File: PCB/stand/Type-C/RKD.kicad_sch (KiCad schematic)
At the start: 65 parts, among them J1 USB_C_Receptacle_USB2.0, J10 Conn_01x04_Male, J11 Conn_02x06_Odd_Even, J12 Conn_01x06, J13 Conn_01x03, J14 Conn_01x04, J15 Conn_01x04, J2 Conn_02x02_Odd_Even, J3 Conn_02x04_Odd_Even, J4 Conn_02x02_Odd_Even, J5 Conn_02x04_Odd_Even, K1 Key, K2 Key, K3 Key, K4 Key, SW2 SW_DIP_x04, SW3 SW_Push, SW5 SW_Push, U1 W25Q32JV, U2 RP2040, U3 CH9329, U4 AMS1117-33, Y1 Crystal 12MHZ HC49, Y2 Crystal_GND24 12MHZ 3225

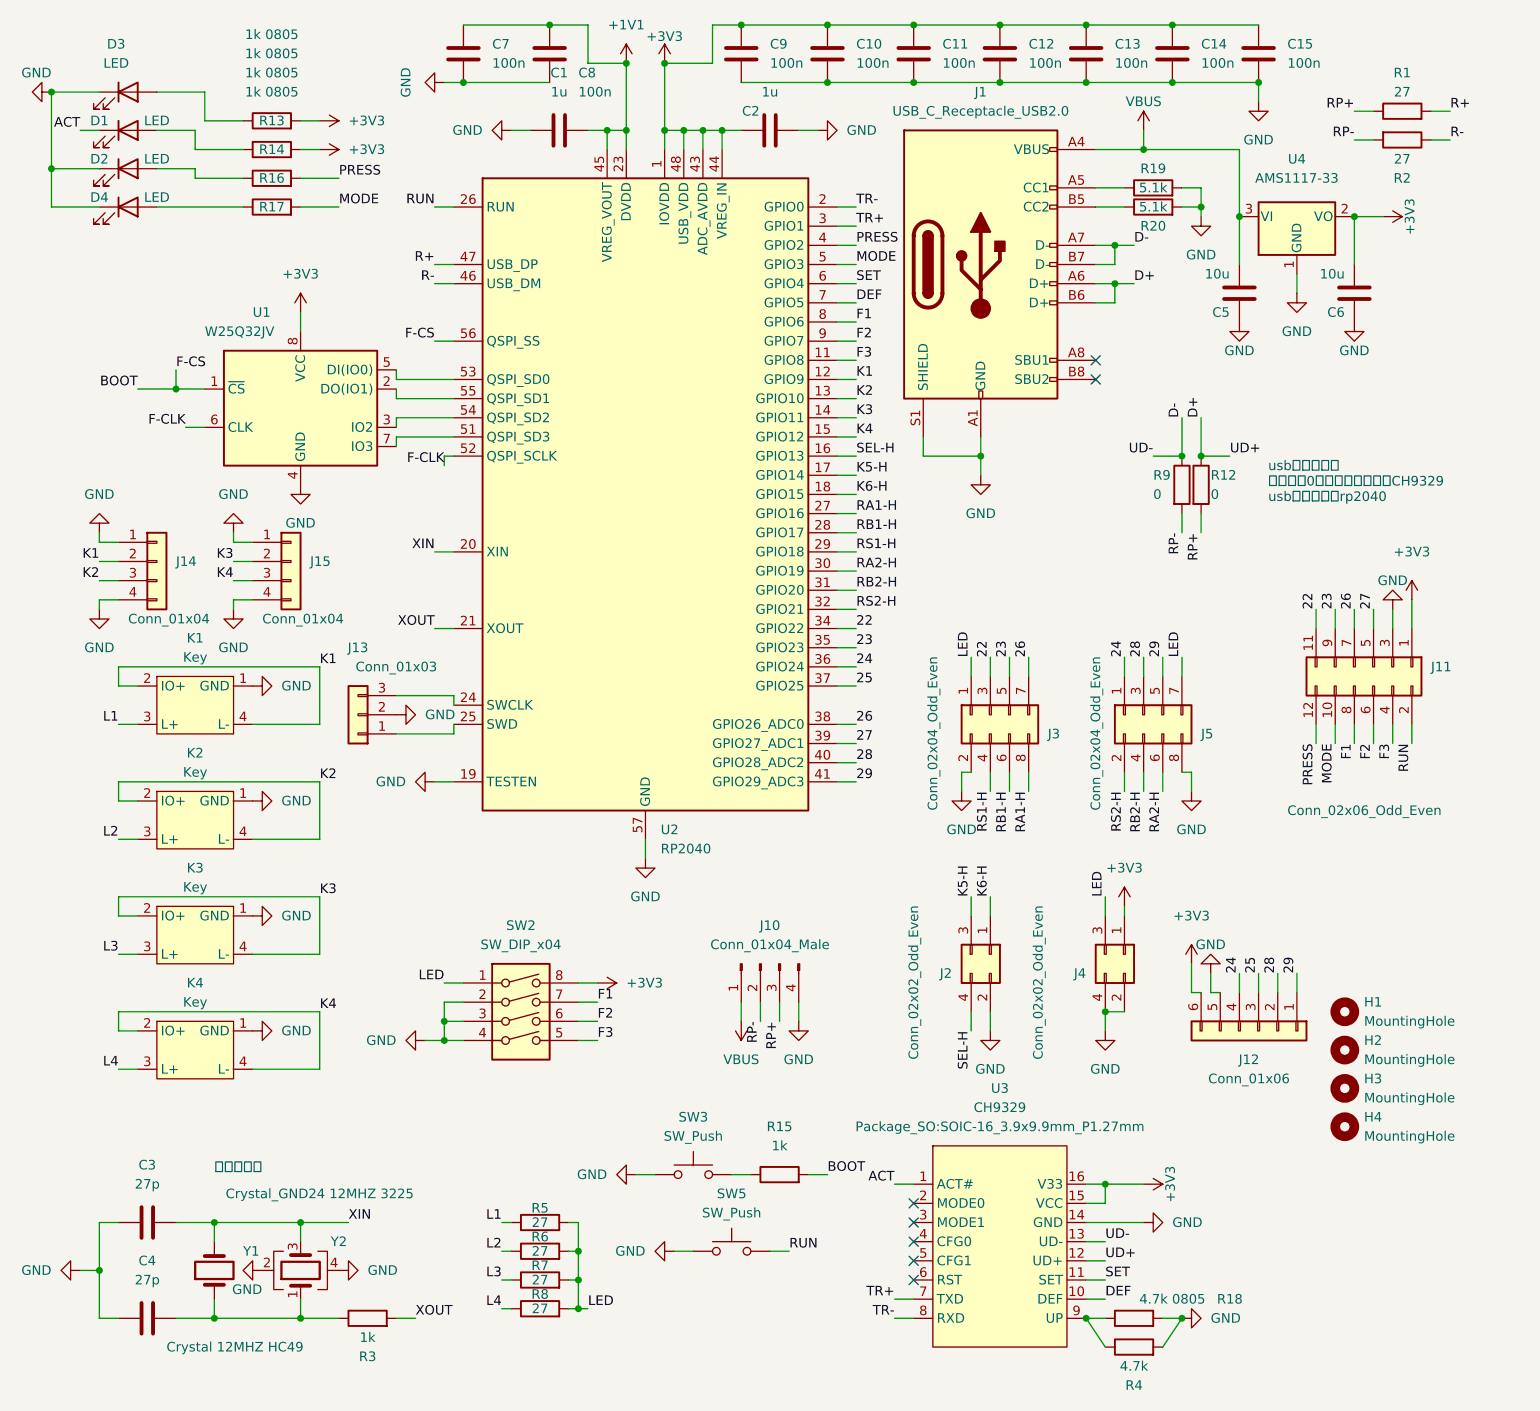
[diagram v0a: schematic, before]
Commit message: 紧急修复:经验证3225晶振无法稳定起振,故去除所以文件中的3225晶振
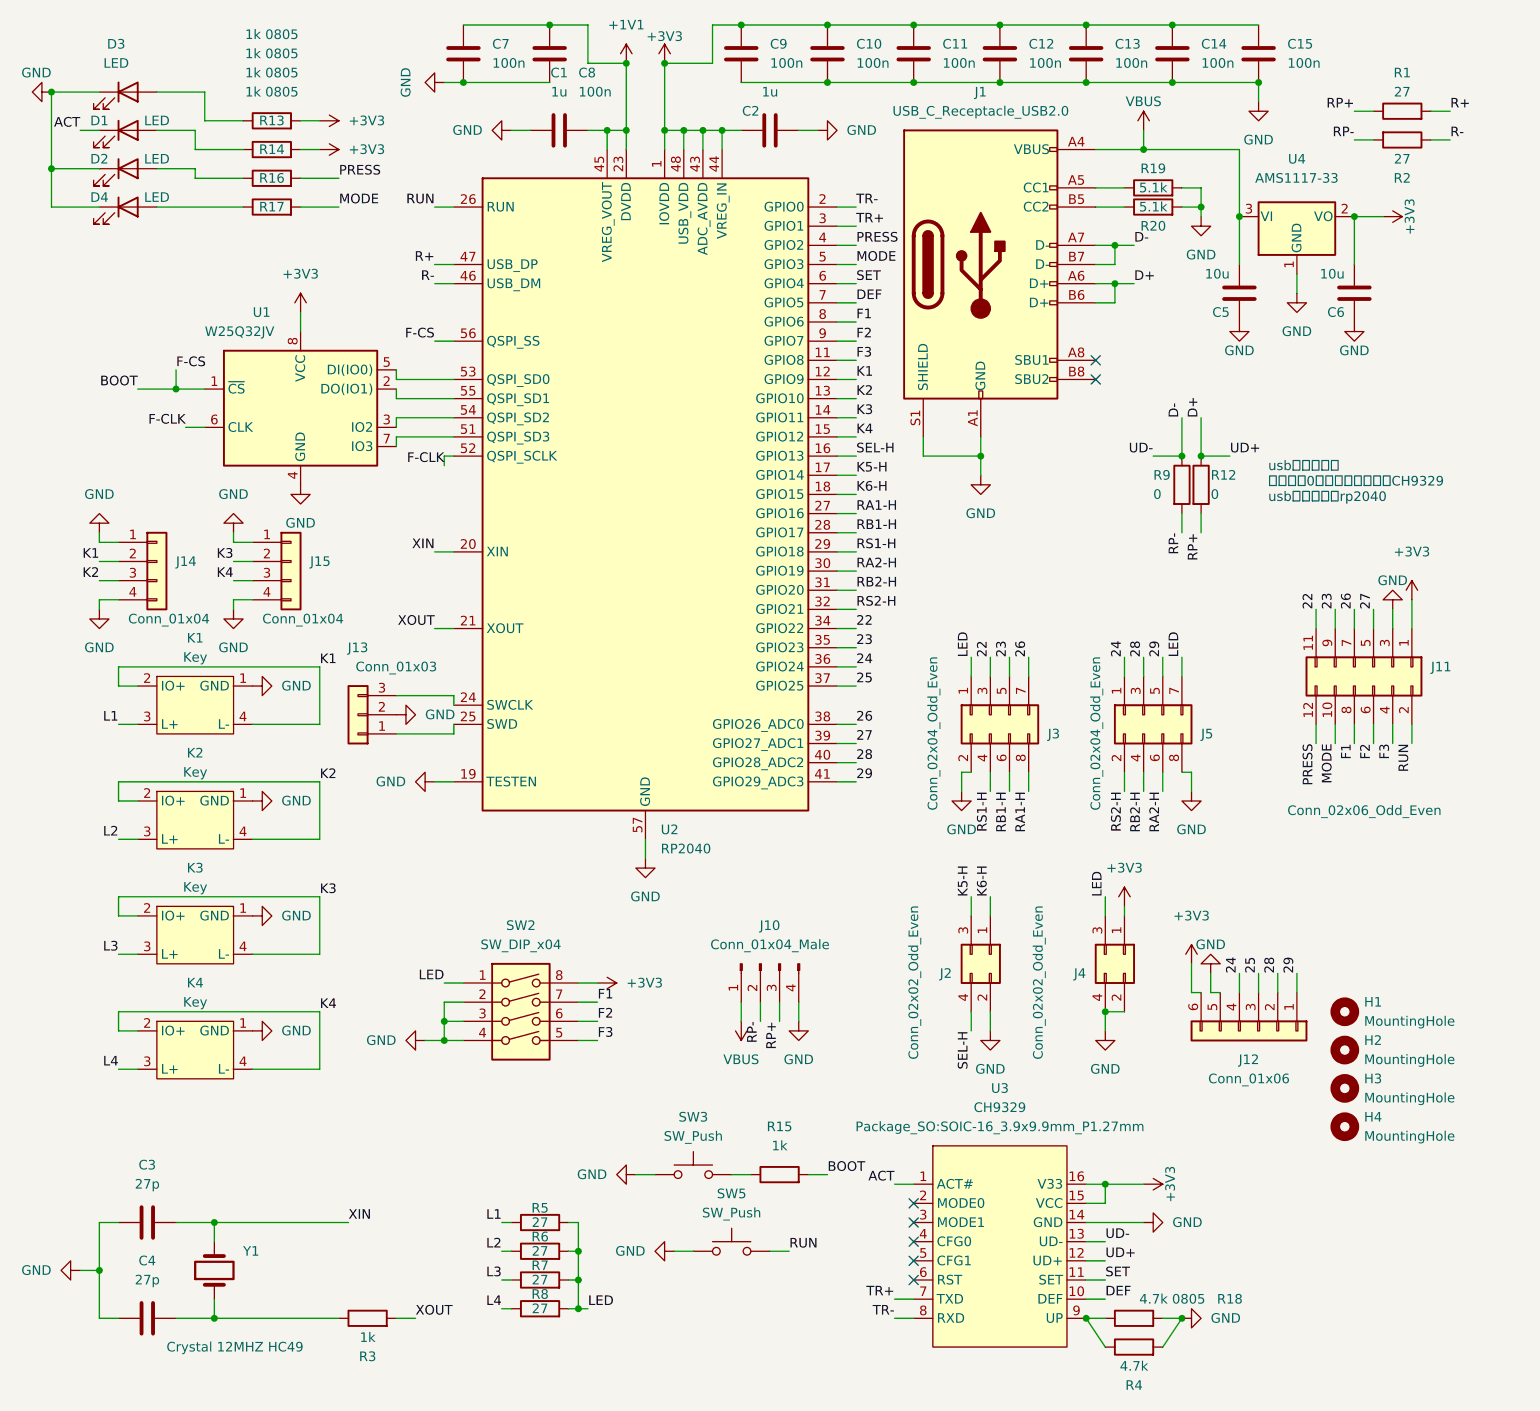
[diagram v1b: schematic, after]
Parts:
- removed Y2: Crystal_GND24 12MHZ 3225, Crystal:Crystal_SMD_3225-4Pin_3.2x2.5mm, symbol Device:Crystal_GND24
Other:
- note removed: "晶振二选一"

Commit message: rename
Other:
- company: PCX-LK -> PTALTS-LK
